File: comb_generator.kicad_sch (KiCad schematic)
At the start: 28 parts, among them J2 RFShield_TwoPieces, U1 ISL3280ExHZ, U4 KT2520K-T, U5 Si5351C-B-GM, U6 GALI-5, U7 PAT1220-C-3DB

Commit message: weiter layoutet...
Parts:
- added C25, C32, C33, C36, C44: 100n, Capacitor_SMD:C_0805_2012Metric_Pad1.18x1.45mm_HandSolder, symbol Device:C_Small
- added C26, C35: 1n, Capacitor_SMD:C_0805_2012Metric_Pad1.18x1.45mm_HandSolder, symbol Device:C_Small
- added C27, C34, C42, C43: 2u2, Capacitor_SMD:C_0805_2012Metric_Pad1.18x1.45mm_HandSolder, symbol Device:C_Small
- added C41: 100p, Capacitor_SMD:C_0805_2012Metric_Pad1.18x1.45mm_HandSolder, symbol Device:C_Small
- added D3: MMD835-0805, Diode_SMD:D_0805_2012Metric_Pad1.15x1.40mm_HandSolder, symbol Device:D_Tunnel
- added FB4: FerriteBead_Small, Inductor_SMD:L_0805_2012Metric_Pad1.15x1.40mm_HandSolder, symbol Device:FerriteBead_Small
- added J11: RFShield_TwoPieces, RF_Shielding:Wuerth_36103305_30x30mm, symbol Device:RFShield_TwoPieces
- added L4, L6: 1uH, Inductor_SMD:L_0805_2012Metric_Pad1.05x1.20mm_HandSolder, symbol Device:L_Small
- added L5: 15uH, Inductor_SMD:L_0805_2012Metric_Pad1.05x1.20mm_HandSolder, symbol Device:L_Small
- added L7: 32n, Inductor_SMD:L_0805_2012Metric_Pad1.05x1.20mm_HandSolder, symbol Device:L_Small
- added L8: 12n7, Inductor_SMD:L_0805_2012Metric_Pad1.05x1.20mm_HandSolder, symbol Device:L_Small
- added R12, R8: 10k, Resistor_SMD:R_0805_2012Metric_Pad1.20x1.40mm_HandSolder, symbol Device:R_Small
- added R13, R7: 470, Resistor_SMD:R_0805_2012Metric_Pad1.20x1.40mm_HandSolder, symbol Device:R_Small
- added R5: 1k5, Resistor_SMD:R_0805_2012Metric_Pad1.20x1.40mm_HandSolder, symbol Device:R_Small
- added RV1, RV2: 10k, Potentiometer_SMD:Potentiometer_Bourns_3214J_Horizontal, symbol Device:R_Potentiometer_Trim
- added U13: PAT1220-C-3DB, RF_Converter:RF_Attenuator_Susumu_PAT1220, symbol RF:PAT1220-C-3DB
- added U2: PHA-13HLN+, Package_TO_SOT_SMD:SOT-89-3, symbol RF_Amplifier:GALI-5
- C1, C10, C11, C2, C3, C4, C5, C6, C9: footprint Capacitor_SMD:C_0603_1608Metric_Pad1.08x0.95mm_HandSolder -> Capacitor_SMD:C_0805_2012Metric_Pad1.18x1.45mm_HandSolder
- C31: renamed from 8p2; value 100n -> 2u2; footprint Capacitor_SMD:C_0603_1608Metric_Pad1.08x0.95mm_HandSolder -> Capacitor_SMD:C_0805_2012Metric_Pad1.18x1.45mm_HandSolder
- C7: value 100n -> 2u2; footprint Capacitor_SMD:C_0603_1608Metric_Pad1.08x0.95mm_HandSolder -> Capacitor_SMD:C_0805_2012Metric_Pad1.18x1.45mm_HandSolder
- C8: value 470p -> 2u2; footprint Capacitor_SMD:C_0603_1608Metric_Pad1.08x0.95mm_HandSolder -> Capacitor_SMD:C_0805_2012Metric_Pad1.18x1.45mm_HandSolder
- D1: value D_Tunnel -> MMD835-0805; Distributor (none) -> Mouser; Distributor PN (none) -> 937-MMD835-0805; Manufacturer (none) -> MACOM; Manufacturer PN (none) -> MMD835-0805
- J2: footprint RF_Shielding:Wuerth_36503305_30x30mm -> RF_Shielding:Wuerth_36103305_30x30mm
- L1: value 1uH -> 15uH
- R1, R2, R3: footprint Resistor_SMD:R_0603_1608Metric_Pad0.98x0.95mm_HandSolder -> Resistor_SMD:R_0805_2012Metric_Pad1.20x1.40mm_HandSolder
- R4: value 68 -> 1k5; footprint Resistor_SMD:R_0603_1608Metric_Pad0.98x0.95mm_HandSolder -> Resistor_SMD:R_0805_2012Metric_Pad1.20x1.40mm_HandSolder
- U6: value GALI-5 -> PHA-13HLN+; Distributor (none) -> Mouser; Distributor PN (none) -> 139-PHA-13HLN; Manufacturer PN (none) -> PHA-13HLN+
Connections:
- net +3V3: no longer R3.1
- net +9VA: now also FB4.2
- net 3V3D: now also R3.1
- net GND: no longer C5.2, C6.2
- net GNDA: now also C5.2, C6.2, D1.1 (K), C26.2, C32.2, C35.2, C36.2, C41.1, C42.2, C44.2, D3.1 (K), J11.1 (Shield), RV1.1, RV2.1, U13.3, U2.2 (GND); no longer D1.2 (A)
- net at U5.12 (CLK1): now also C27.1
- net at C7.2, U6.1: now also C25.1
- net at C8.1, L1.2, U6.3: now also R5.2
- net at C31.2, L3.2: now also D1.2 (A); no longer D1.1 (K)
- net at C8.2, L2.1: now also L4.2
- net at C5.1, C6.1, FB2.1: now also L1.1, C26.1, R12.2; no longer R4.1
- net at R4.2: now also C34.1, L5.2, U2.3; no longer L1.1
- net comb_out renamed comb_out_1
- new net: C25.2, R5.1
- new net: C34.2, L6.2, L7.1
- new net: C41.2, L7.2, L8.1
- new net: C36.1, R7.2, RV2.2
- new net: R8.1, RV2.3
- new net: C43.2, D3.2 (A), L8.2
- new net: C35.1, C42.1, C44.1, FB4.1, L5.1, R8.2
- new net: L6.1, R7.1
- new net: C43.1, U13.1
- new net: C32.1, R13.2, RV1.2
- new net: L4.1, R13.1
- new net: C27.2, C33.1, U2.1
- new net: C33.2, R4.1
- new net: R12.1, RV1.3
- new net comb_out_2: U13.2
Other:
- moved on the sheet: C1, C10, C11, C2, C3, C31, C4, C5, C6, C7, C8, C9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

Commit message: es wird langsam...
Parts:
- added C47, C48, C49, C50: 100n, Capacitor_SMD:C_0805_2012Metric_Pad1.18x1.45mm_HandSolder, symbol Device:C_Small
- J11, J2: footprint RF_Shielding:Wuerth_36103305_30x30mm -> RF_Shielding:Wuerth_3670473_47.3x23.3
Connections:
- net GNDA is gone; now on net GND: C26.2, C32.2, C35.2, C36.2, C41.1, C42.2, C44.2, C5.2, C6.2, C9.1, D1.1 (K), D3.1 (K), J11.1 (Shield), J2.1 (Shield), RV1.1, RV2.1, U13.3, U2.2 (GND), U6.2 (GND), U7.3
- net GND: now also C47.2, C48.2, C49.2, C50.2
- net at U5.12 (CLK1): no longer C27.1
- net CLK0: now reaches U5.13 (CLK0)
- net CLK0: now also C27.1; no longer C7.1
- net CLK1: now reaches U5.15 (CLK7)
- net CLK1: now also C7.1
- net at C35.1, C42.1, C44.1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: now also C47.1, C48.1
- net at C26.1, C5.1, C6.1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: now also C49.1, C50.1
- no-connect marks 8 -> 7

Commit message: BOM angefangen und im Layout vom Hundertsten ins Tausendste gekommen...
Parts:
- removed U4: KT2520K-T, Oscillator:Oscillator_SMD_Kyocera_2520-6Pin_2.5x2.0mm, symbol Oscillator:KT2520K-T
- added Y2: TG2520SMN-xx.xxxxxxMhz-xxxxNM, Oscillator:Oscillator_SMD_SeikoEpson_TG2520SMN-xxx-xxxxxx-4Pin_2.5x2.0mm, symbol Oscillator:TG2520SMN-xx.xxxxxxMhz-xxxxNM
- C1, C10, C11, C25, C32, C33, C36, C4, C44, C47, C48, C49, C50, C6: Distributor (none) -> Mouser; Distributor PN (none) -> 581-KAM21BR71H104JT; Manufacturer (none) -> KYOCERA AVX; Manufacturer PN (none) -> KAM21BR71H104JT
- C2, C27, C3, C31, C34, C42, C43, C5, C7, C8: Distributor (none) -> Mouser; Distributor PN (none) -> 581-KAM21KR71E225KU; Manufacturer (none) -> KYOCERA AVX; Manufacturer PN (none) -> KAM21KR71E225KU
- J11, J2: Distributor (none) -> Mouser; Distributor PN (none) -> 710-3670473; Manufacturer (none) -> Wurth Elektronik; Manufacturer PN (none) -> 3670473
- RV1, RV2: footprint Potentiometer_SMD:Potentiometer_Bourns_3214J_Horizontal -> Potentiometer_SMD:Potentiometer_Bourns_TC33X_Vertical
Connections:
- net 3V3D: now also Y2.4 (Vcc)
- net GND: now also Y2.2 (GND)
- net at U5.1 (XA): now also Y2.3 (OUT)

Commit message: BOM...
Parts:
- RV1, RV2: Distributor (none) -> Mouser; Distributor PN (none) -> 652-TC33X-2-103E; Manufacturer (none) -> Bourns; Manufacturer PN (none) -> TC33X-2-103E
- U1: Distributor (none) -> Mouser; Distributor PN (none) -> 968-ISL3280EIHZ-T; Manufacturer (none) -> Renesas / Intersil; Manufacturer PN (none) -> ISL3280EIHZ-T
- U13, U7: Distributor (none) -> Mouser; Distributor PN (none) -> 754-PAT1220C-3DBT5; Manufacturer (none) -> Susumu; Manufacturer PN (none) -> PAT1220-C-3DB-T5
- U2, U6: Manufacturer (none) -> Mini-Circuits
- U5: Distributor (none) -> Mouser; Distributor PN (none) -> 634-SI5351C-B-GM; Manufacturer (none) -> Skyworks Solutions, Inc.; Manufacturer PN (none) -> SI5351C-B-GM
- Y2: Distributor (none) -> Mouser; Distributor PN (none) -> 732-TG252S25MCGNNM3; Manufacturer (none) -> Epson; Manufacturer PN (none) -> TG2520SMN 25.000M-MCGNNM3
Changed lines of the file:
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@@
 			)
 		)
+		(property "Distributor" "Mouser"
+			(at 74.93 88.9 0)
+			(effects
+				(font
+					(size 1.27 1.27)
+				)
+			)
+		)
+		(property "Distributor PN" "968-ISL3280EIHZ-T "
+			(at 74.93 88.9 0)
+			(effects
+				(font
+					(size 1.27 1.27)
+				)
+			)
+		)
+		(property "Manufacturer" "Renesas / Intersil "
+			(at 74.93 88.9 0)
+			(effects
+				(font
+					(size 1.27 1.27)
+				)
+			)
+		)
+		(property "Manufacturer PN" "ISL3280EIHZ-T "
+			(at 74.93 88.9 0)
+			(effects
+				(font
+					(size 1.27 1.27)
+				)
+			)
+		)
 		(pin "5"
 		)
@@
 			)
 		)
+		(property "Distributor" "Mouser"
+			(at 74.93 58.42 0)
+			(effects
+				(font
+					(size 1.27 1.27)
+				)
+			)
+		)
+		(property "Distributor PN" " 732-TG252S25MCGNNM3 "
+			(at 74.93 58.42 0)
+			(effects
+				(font
+					(size 1.27 1.27)
+				)
+			)
+		)
+		(property "Manufacturer" "Epson"
+			(at 74.93 58.42 0)
+			(effects
+				(font
+					(size 1.27 1.27)
+				)
+			)
+		)
+		(property "Manufacturer PN" "TG2520SMN 25.000M-MCGNNM3"
+			(at 74.93 58.42 0)
+			(effects
+				(font
+					(size 1.27 1.27)
+				)
+			)
+		)
 		(pin "2"
 		)
@@
 			)
 		)
+		(property "Distributor" "Mouser"
+			(at 115.57 93.98 0)
+			(effects
+				(font
+					(size 1.27 1.27)
+				)
+			)
+		)
+		(property "Distributor PN" " 634-SI5351C-B-GM "
+			(at 115.57 93.98 0)
+			(effects
+				(font
+					(size 1.27 1.27)
+				)
+			)
+		)
+		(property "Manufacturer" "Skyworks Solutions, Inc. "
+			(at 115.57 93.98 0)
+			(effects
+				(font
+					(size 1.27 1.27)
+				)
+			)
+		)
+		(property "Manufacturer PN" "SI5351C-B-GM"
+			(at 115.57 93.98 0)
+			(effects
+				(font
+					(size 1.27 1.27)
+				)
+			)
+		)
 		(pin "9"
 		)
@@
 			)
 		)
-		(property "Manufacturer PN" ""
+		(property "Manufacturer PN" "TC33X-2-103E"
 			(at 209.55 118.11 0)
 			(effects
@@
 			)
 		)
-		(property "Manufacturer" ""
+		(property "Manufacturer" "Bourns "
 			(at 209.55 118.11 0)
 			(effects
@@
 			)
 		)
-		(property "Distributor" ""
+		(property "Distributor" "Mouser"
 			(at 209.55 118.11 0)
 			(effects
@@
 			)
 		)
-		(property "Distributor PN" ""
+		(property "Distributor PN" " 652-TC33X-2-103E "
 			(at 209.55 118.11 0)
 			(effects
@@
 			)
 		)
-		(property "Manufacturer" ""
+		(property "Manufacturer" "Mini-Circuits"
 			(at 170.18 76.2 0)
 			(effects
@@
 			)
 		)
+		(property "Distributor" "Mouser"
+			(at 247.65 138.43 0)
+			(effects
+				(font
+					(size 1.27 1.27)
+				)
+			)
+		)
+		(property "Distributor PN" " 754-PAT1220C-3DBT5 "
+			(at 247.65 138.43 0)
+			(effects
+				(font
+					(size 1.27 1.27)
+				)
+			)
+		)
+		(property "Manufacturer" "Susumu "
+			(at 247.65 138.43 0)
+			(effects
+				(font
+					(size 1.27 1.27)
+				)
+			)
+		)
+		(property "Manufacturer PN" "PAT1220-C-3DB-T5"
+			(at 247.65 138.43 0)
+			(effects
+				(font
+					(size 1.27 1.27)
+				)
+			)
+		)
 		(pin "1"
 		)
@@
 			)
 		)
-		(property "Manufacturer PN" ""
+		(property "Manufacturer PN" "TC33X-2-103E"
 			(at 209.55 58.42 0)
 			(effects
@@
 			)
 		)
-		(property "Manufacturer" ""
+		(property "Manufacturer" "Bourns "
 			(at 209.55 58.42 0)
 			(effects
@@
 			)
 		)
-		(property "Distributor" ""
+		(property "Distributor" "Mouser"
 			(at 209.55 58.42 0)
 			(effects
@@
 			)
 		)
-		(property "Distributor PN" ""
+		(property "Distributor PN" " 652-TC33X-2-103E "
 			(at 209.55 58.42 0)
 			(effects
@@
 			)
 		)
-		(property "Manufacturer" ""
+		(property "Manufacturer" "Mini-Circuits"
 			(at 170.18 135.89 0)
 			(effects
@@
 			)
 		)
+		(property "Distributor" "Mouser"
+			(at 247.65 78.74 0)
+			(effects
+				(font
+					(size 1.27 1.27)
+				)
+			)
+		)
+		(property "Distributor PN" " 754-PAT1220C-3DBT5 "
+			(at 247.65 78.74 0)
+			(effects
+				(font
+					(size 1.27 1.27)
+				)
+			)
+		)
+		(property "Manufacturer" "Susumu "
+			(at 247.65 78.74 0)
+			(effects
+				(font
+					(size 1.27 1.27)
+				)
+			)
+		)
+		(property "Manufacturer PN" "PAT1220-C-3DB-T5"
+			(at 247.65 78.74 0)
+			(effects
+				(font
+					(size 1.27 1.27)
+				)
+			)
+		)

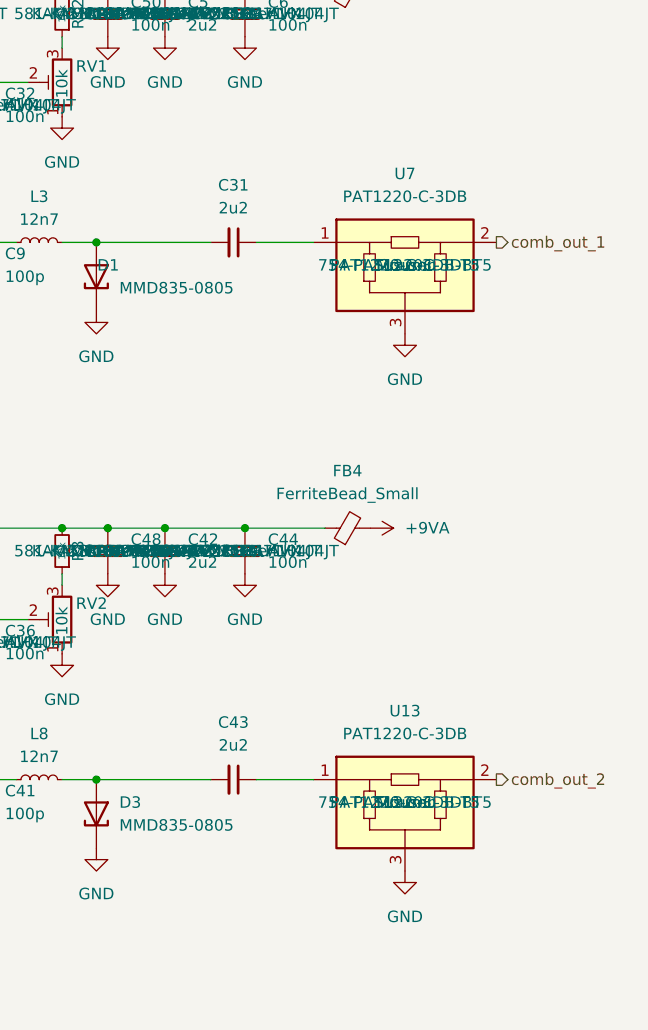
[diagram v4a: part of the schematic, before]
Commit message: got samples von Minicircuits, change attenuator to GAT-x
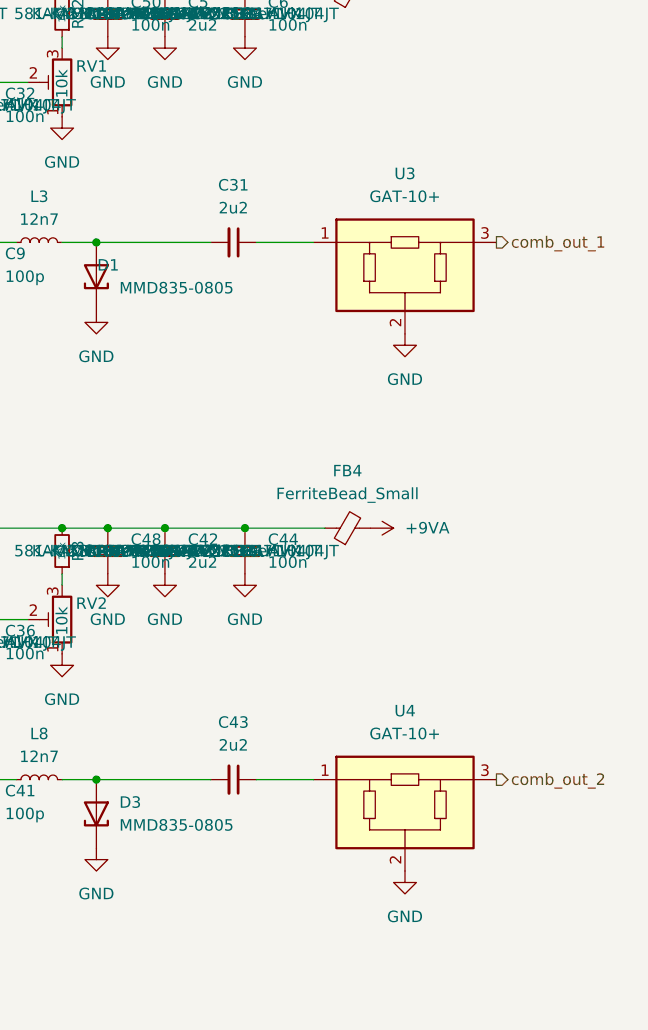
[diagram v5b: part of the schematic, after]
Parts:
- removed U13, U7: PAT1220-C-3DB, RF_Converter:RF_Attenuator_Susumu_PAT1220, symbol RF:PAT1220-C-3DB
- added U3, U4: GAT-10+, Package_DFN_QFN:Mini-Circuits_FG873-4_3x3mm, symbol RF:GAT-10
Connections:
- net GND: now also U3.2, U3.4, U4.2, U4.4
- net comb_out_1: now also U3.3
- net comb_out_2: now also U4.3
- net at C43.1: now also U4.1
- net at C31.1: now also U3.1
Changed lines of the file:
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@@
 	)
 	(symbol
+		(lib_id "RF:GAT-10")
+		(at 247.65 138.43 0)
+		(unit 1)
+		(exclude_from_sim no)
+		(in_bom yes)
+		(on_board yes)
+		(dnp no)
+		(fields_autoplaced yes)
+		(property "Reference" "U4"
+			(at 247.65 128.27 0)
+			(effects
+				(font
+					(size 1.27 1.27)
+				)
+			)
+		)
+		(property "Value" "GAT-10+"
+			(at 247.65 130.81 0)
+			(effects
+				(font
+					(size 1.27 1.27)
+				)
+			)
+		)
+		(property "Footprint" "Package_DFN_QFN:Mini-Circuits_FG873-4_3x3mm"
+			(at 247.65 138.43 0)
+			(effects
+				(font
+					(size 1.27 1.27)
+				)
+				(hide yes)
+			)
+		)
+		(property "Datasheet" "https://www.minicircuits.com/pdfs/GAT-10+.pdf"
+			(at 241.3 132.08 0)
+			(effects
+				(font
+					(size 1.27 1.27)
+				)
+				(hide yes)
+			)
+		)
+		(property "Description" "8GHz RF Attenuator, 50ohm Matched Impedance, 10dB Attenuation, GAT-10"
+			(at 247.65 138.43 0)
+			(effects
+				(font
+					(size 1.27 1.27)
+				)
+				(hide yes)
+			)
+		)
+		(property "Manufacturer PN" ""
+			(at 247.65 138.43 0)
+			(effects
+				(font
+					(size 1.27 1.27)
+				)
+				(hide yes)
+			)
+		)
+		(property "Manufacturer" ""
+			(at 247.65 138.43 0)
+			(effects
+				(font
+					(size 1.27 1.27)
+				)
+				(hide yes)
+			)
+		)
+		(property "Distributor" ""
+			(at 247.65 138.43 0)
+			(effects
+				(font
+					(size 1.27 1.27)
+				)
+				(hide yes)
+			)
+		)
+		(property "Distributor PN" ""
+			(at 247.65 138.43 0)
+			(effects
+				(font
+					(size 1.27 1.27)
+				)
+				(hide yes)
+			)
+		)
+		(pin "3"
+		)
+		(pin "4"
+		)
+		(pin "2"
+		)
+		(pin "1"
+		)
+		(instances
+			(project "SI5351_broadband_comb_generatror"
+				(path "/e3ffa783-81af-49ae-8254-21eed35dbc9d/daa18232-54a7-4b4b-bed2-249a906eef53"
+					(reference "U4")
+					(unit 1)
+				)
+			)
+		)
+	)
+	(symbol
 		(lib_id "power:+3V3")
 		(at 110.49 50.8 0)
@@
 	)
 	(symbol
-		(lib_id "RF:PAT1220-C-3DB")
-		(at 247.65 138.43 0)
-		(unit 1)
-		(exclude_from_sim no)
-		(in_bom yes)
-		(on_board yes)
-		(dnp no)
-		(fields_autoplaced yes)
-		(property "Reference" "U13"
-			(at 247.65 128.27 0)
-			(effects
-				(font
-					(size 1.27 1.27)
-				)
-			)
-		)
-		(property "Value" "PAT1220-C-3DB"
-			(at 247.65 130.81 0)
-			(effects
-				(font
-					(size 1.27 1.27)
-				)
-			)
-		)
-		(property "Footprint" "RF_Converter:RF_Attenuator_Susumu_PAT1220"
-			(at 247.65 138.43 0)
-			(effects
-				(font
-					(size 1.27 1.27)
-				)
-				(hide yes)
-			)
-		)
-		(property "Datasheet" "https://www.susumu.co.jp/common/pdf/n_catalog_partition16_en.pdf"
-			(at 241.3 132.08 0)
-			(effects
-				(font
-					(size 1.27 1.27)
-				)
-				(hide yes)
-			)
-		)
-		(property "Description" "10GHz RF Attenuator, 50ohm Matched Impedance, 3dB Attenuation, PAT1220"
-			(at 247.65 138.43 0)
-			(effects
-				(font
-					(size 1.27 1.27)
-				)
-				(hide yes)
-			)
-		)
-		(property "Distributor" "Mouser"
-			(at 247.65 138.43 0)
-			(effects
-				(font
-					(size 1.27 1.27)
-				)
-			)
-		)
-		(property "Distributor PN" " 754-PAT1220C-3DBT5 "
-			(at 247.65 138.43 0)
-			(effects
-				(font
-					(size 1.27 1.27)
-				)
-			)
-		)
-		(property "Manufacturer" "Susumu "
-			(at 247.65 138.43 0)
-			(effects
-				(font
-					(size 1.27 1.27)
-				)
-			)
-		)
-		(property "Manufacturer PN" "PAT1220-C-3DB-T5"
-			(at 247.65 138.43 0)
-			(effects
-				(font
-					(size 1.27 1.27)
-				)
-			)
-		)
-		(pin "1"
-		)
-		(pin "3"
-		)
-		(pin "2"
-		)
-		(instances
-			(project "SI5351_broadband_comb_generatror"
-				(path "/e3ffa783-81af-49ae-8254-21eed35dbc9d/daa18232-54a7-4b4b-bed2-249a906eef53"
-					(reference "U13")
-					(unit 1)
-				)
-			)
-		)
-	)
-	(symbol
 		(lib_id "power:GND")
 		(at 58.42 96.52 0)
@@
 	)
 	(symbol
-		(lib_id "RF:PAT1220-C-3DB")
-		(at 247.65 78.74 0)
-		(unit 1)
-		(exclude_from_sim no)
-		(in_bom yes)
-		(on_board yes)
-		(dnp no)
-		(fields_autoplaced yes)
-		(property "Reference" "U7"
-			(at 247.65 68.58 0)
-			(effects
-				(font
-					(size 1.27 1.27)
-				)
-			)
-		)
-		(property "Value" "PAT1220-C-3DB"
-			(at 247.65 71.12 0)
-			(effects
-				(font
-					(size 1.27 1.27)
-				)
-			)
-		)
-		(property "Footprint" "RF_Converter:RF_Attenuator_Susumu_PAT1220"
-			(at 247.65 78.74 0)
-			(effects
-				(font
-					(size 1.27 1.27)
-				)
-				(hide yes)
-			)
-		)
-		(property "Datasheet" "https://www.susumu.co.jp/common/pdf/n_catalog_partition16_en.pdf"
-			(at 241.3 72.39 0)
-			(effects
-				(font
-					(size 1.27 1.27)
-				)
-				(hide yes)
-			)
-		)
-		(property "Description" "10GHz RF Attenuator, 50ohm Matched Impedance, 3dB Attenuation, PAT1220"
-			(at 247.65 78.74 0)
-			(effects
-				(font
-					(size 1.27 1.27)
-				)
-				(hide yes)
-			)
-		)
-		(property "Distributor" "Mouser"
-			(at 247.65 78.74 0)
-			(effects
-				(font
-					(size 1.27 1.27)
-				)
-			)
-		)
-		(property "Distributor PN" " 754-PAT1220C-3DBT5 "
-			(at 247.65 78.74 0)
-			(effects
-				(font
-					(size 1.27 1.27)
-				)
-			)
-		)
-		(property "Manufacturer" "Susumu "
-			(at 247.65 78.74 0)
-			(effects
-				(font
-					(size 1.27 1.27)
-				)
-			)
-		)
-		(property "Manufacturer PN" "PAT1220-C-3DB-T5"
-			(at 247.65 78.74 0)
-			(effects
-				(font
-					(size 1.27 1.27)
-				)
-			)
-		)
-		(pin "1"
-		)
-		(pin "3"
-		)
-		(pin "2"
-		)
-		(instances
-			(project ""
-				(path "/e3ffa783-81af-49ae-8254-21eed35dbc9d/daa18232-54a7-4b4b-bed2-249a906eef53"
-					(reference "U7")
-					(unit 1)
-				)
-			)
-		)
-	)
-	(symbol
 		(lib_id "power:GND")
 		(at 87.63 68.58 0)
@@
 					(unit 1)
 				)
+			)
+		)
+	)
+	(symbol
+		(lib_id "RF:GAT-10")
+		(at 247.65 78.74 0)
+		(unit 1)
+		(exclude_from_sim no)
+		(in_bom yes)
+		(on_board yes)
+		(dnp no)
+		(fields_autoplaced yes)
+		(property "Reference" "U3"
+			(at 247.65 68.58 0)
+			(effects
+				(font
+					(size 1.27 1.27)
+				)
+			)
+		)
+		(property "Value" "GAT-10+"
+			(at 247.65 71.12 0)
+			(effects
+				(font
+					(size 1.27 1.27)
+				)
+			)
+		)
+		(property "Footprint" "Package_DFN_QFN:Mini-Circuits_FG873-4_3x3mm"
+			(at 247.65 78.74 0)
+			(effects
+				(font
+					(size 1.27 1.27)
+				)
+				(hide yes)
+			)
+		)
+		(property "Datasheet" "https://www.minicircuits.com/pdfs/GAT-10+.pdf"
+			(at 241.3 72.39 0)
+			(effects
+				(font
+					(size 1.27 1.27)
+				)
+				(hide yes)
+			)
+		)
+		(property "Description" "8GHz RF Attenuator, 50ohm Matched Impedance, 10dB Attenuation, GAT-10"
+			(at 247.65 78.74 0)
+			(effects
+				(font
+					(size 1.27 1.27)
+				)
+				(hide yes)
+			)
+		)
+		(property "Manufacturer PN" ""
+			(at 247.65 78.74 0)
+			(effects
+				(font
+					(size 1.27 1.27)
+				)
+				(hide yes)
+			)
+		)
+		(property "Manufacturer" ""
+			(at 247.65 78.74 0)
+			(effects
+				(font
+					(size 1.27 1.27)
+				)
+				(hide yes)
+			)
+		)
+		(property "Distributor" ""
+			(at 247.65 78.74 0)
+			(effects
+				(font
+					(size 1.27 1.27)
+				)
+				(hide yes)
+			)
+		)
+		(property "Distributor PN" ""
+			(at 247.65 78.74 0)
+			(effects
+				(font
+					(size 1.27 1.27)
+				)
+				(hide yes)
+			)
+		)
+		(pin "3"
+		)
+		(pin "4"
+		)
+		(pin "2"
+		)
+		(pin "1"
+		)
+		(instances
+			(project ""
+				(path "/e3ffa783-81af-49ae-8254-21eed35dbc9d/daa18232-54a7-4b4b-bed2-249a906eef53"
+					(reference "U3")
+					(unit 1)
+				)
